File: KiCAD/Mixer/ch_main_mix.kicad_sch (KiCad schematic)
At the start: 1 part, among them U4 NE5532

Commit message: Power Bus, Footprints, Audio Bus
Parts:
- U4: footprint (none) -> Package_SO:SOIC-8_3.9x4.9mm_P1.27mm
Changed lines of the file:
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@@
 			)
 		)
-		(property "Footprint" ""
+		(property "Footprint" "Package_SO:SOIC-8_3.9x4.9mm_P1.27mm"
 			(at 60.96 88.9 0)
 			(hide yes)
@@
 			)
 		)
-		(property "Footprint" ""
+		(property "Footprint" "Package_SO:SOIC-8_3.9x4.9mm_P1.27mm"
 			(at 49.53 49.53 0)
 			(hide yes)
@@
 			)
 		)
-		(property "Footprint" ""
+		(property "Footprint" "Package_SO:SOIC-8_3.9x4.9mm_P1.27mm"
 			(at 60.96 76.2 0)
 			(hide yes)

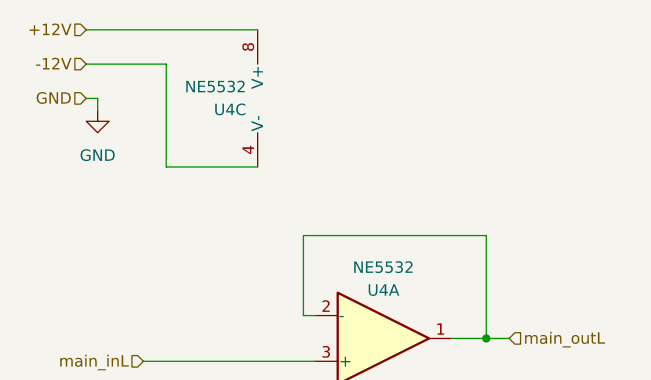
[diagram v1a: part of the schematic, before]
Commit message: added second channel and footprints / created PCB desing...might make PCB bit bigger
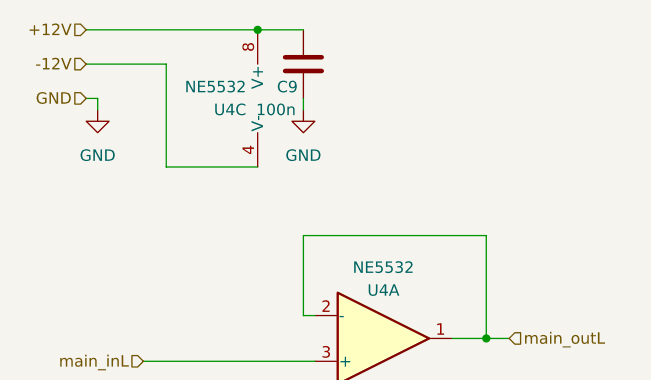
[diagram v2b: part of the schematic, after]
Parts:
- added C9: 100n, Capacitor_SMD:C_0805_2012Metric_Pad1.18x1.45mm_HandSolder, symbol Device:C
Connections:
- net +12V: now also C9.2
- net GND: now also C9.1
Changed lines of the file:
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@@
+	)
+	(junction
+		(at 46.99 41.91)
+		(diameter 0)
+		(color 0 0 0 0)
 	)
 	(junction
@@
 	(wire
 		(pts
+			(xy 46.99 41.91) (xy 52.07 41.91)
+		)
+		(stroke
+			(width 0)
+			(type default)
+		)
+	)
+	(wire
+		(pts
 			(xy 68.58 88.9) (xy 72.39 88.9)
 		)
@@
 		(pts
 			(xy 36.83 57.15) (xy 46.99 57.15)
+		)
+		(stroke
+			(width 0)
+			(type default)
+		)
+	)
+	(wire
+		(pts
+			(xy 52.07 49.53) (xy 52.07 50.8)
 		)
 		(stroke
@@
 		(instances
 			(project "Mixer"
+				(path "/322d427a-6aae-4762-92d6-d97688daf29b/8a2849b7-184d-4014-bb98-da9dec8b5f90/63151d98-ae0a-469c-944a-54e511d723e3"
+					(reference "U6")
+					(unit 2)
+				)
 				(path "/322d427a-6aae-4762-92d6-d97688daf29b/8a2849b7-184d-4014-bb98-da9dec8b5f90/8a6fa50f-425a-481d-926c-437edf9380b2"
 					(reference "U4")
@@
 		(instances
 			(project "Mixer"
+				(path "/322d427a-6aae-4762-92d6-d97688daf29b/8a2849b7-184d-4014-bb98-da9dec8b5f90/63151d98-ae0a-469c-944a-54e511d723e3"
+					(reference "U6")
+					(unit 3)
+				)
 				(path "/322d427a-6aae-4762-92d6-d97688daf29b/8a2849b7-184d-4014-bb98-da9dec8b5f90/8a6fa50f-425a-481d-926c-437edf9380b2"
 					(reference "U4")
 					(unit 3)
+				)
+			)
+		)
+	)
+	(symbol
+		(lib_id "power:GND")
+		(at 52.07 50.8 0)
+		(unit 1)
+		(body_style 1)
+		(exclude_from_sim no)
+		(in_bom yes)
+		(on_board yes)
+		(in_pos_files yes)
+		(dnp no)
+		(fields_autoplaced yes)
+		(property "Reference" "#PWR097"
+			(at 52.07 57.15 0)
+			(hide yes)
+			(show_name no)
+			(do_not_autoplace no)
+			(effects
+				(font
+					(size 1.27 1.27)
+				)
+			)
+		)
+		(property "Value" "GND"
+			(at 52.07 55.88 0)
+			(show_name no)
+			(do_not_autoplace no)
+			(effects
+				(font
+					(size 1.27 1.27)
+				)
+			)
+		)
+		(property "Footprint" ""
+			(at 52.07 50.8 0)
+			(hide yes)
+			(show_name no)
+			(do_not_autoplace no)
+			(effects
+				(font
+					(size 1.27 1.27)
+				)
+			)
+		)
+		(property "Datasheet" ""
+			(at 52.07 50.8 0)
+			(hide yes)
+			(show_name no)
+			(do_not_autoplace no)
+			(effects
+				(font
+					(size 1.27 1.27)
+				)
+			)
+		)
+		(property "Description" "Power symbol creates a global label with name \"GND\" , ground"
+			(at 52.07 50.8 0)
+			(hide yes)
+			(show_name no)
+			(do_not_autoplace no)
+			(effects
+				(font
+					(size 1.27 1.27)
+				)
+			)
+		)
+		(pin "1"
+		)
+		(instances
+			(project "Mixer"
+				(path "/322d427a-6aae-4762-92d6-d97688daf29b/8a2849b7-184d-4014-bb98-da9dec8b5f90/63151d98-ae0a-469c-944a-54e511d723e3"
+					(reference "#PWR098")
+					(unit 1)
+				)
+				(path "/322d427a-6aae-4762-92d6-d97688daf29b/8a2849b7-184d-4014-bb98-da9dec8b5f90/8a6fa50f-425a-481d-926c-437edf9380b2"
+					(reference "#PWR097")
+					(unit 1)
 				)
 			)
@@
 		(instances
 			(project "Mixer"
+				(path "/322d427a-6aae-4762-92d6-d97688daf29b/8a2849b7-184d-4014-bb98-da9dec8b5f90/63151d98-ae0a-469c-944a-54e511d723e3"
+					(reference "U6")
+					(unit 1)
+				)
 				(path "/322d427a-6aae-4762-92d6-d97688daf29b/8a2849b7-184d-4014-bb98-da9dec8b5f90/8a6fa50f-425a-481d-926c-437edf9380b2"
 					(reference "U4")
@@
 		(instances
 			(project "Mixer"
+				(path "/322d427a-6aae-4762-92d6-d97688daf29b/8a2849b7-184d-4014-bb98-da9dec8b5f90/63151d98-ae0a-469c-944a-54e511d723e3"
+					(reference "#PWR094")
+					(unit 1)
+				)
 				(path "/322d427a-6aae-4762-92d6-d97688daf29b/8a2849b7-184d-4014-bb98-da9dec8b5f90/8a6fa50f-425a-481d-926c-437edf9380b2"
 					(reference "#PWR022")
 					(unit 1)
 				)
+			)
+		)
+	)
+	(symbol
+		(lib_id "Device:C")
+		(at 52.07 45.72 180)
+		(unit 1)
+		(body_style 1)
+		(exclude_from_sim no)
+		(in_bom yes)
+		(on_board yes)
+		(in_pos_files yes)
+		(dnp no)
+		(property "Reference" "C9"
+			(at 50.292 48.26 0)
+			(show_name no)
+			(do_not_autoplace no)
+			(effects
+				(font
+					(size 1.27 1.27)
+				)
+			)
+		)
+		(property "Value" "100n"
+			(at 49.022 50.8 0)
+			(show_name no)
+			(do_not_autoplace no)
+			(effects
+				(font
+					(size 1.27 1.27)
+				)
+			)
+		)
+		(property "Footprint" "Capacitor_SMD:C_0805_2012Metric_Pad1.18x1.45mm_HandSolder"
+			(at 51.1048 41.91 0)
+			(hide yes)
+			(show_name no)
+			(do_not_autoplace no)
+			(effects
+				(font
+					(size 1.27 1.27)
+				)
+			)
+		)
+		(property "Datasheet" ""
+			(at 52.07 45.72 0)
+			(hide yes)
+			(show_name no)
+			(do_not_autoplace no)
+			(effects
+				(font
+					(size 1.27 1.27)
+				)
+			)
+		)
+		(property "Description" "Unpolarized capacitor"
+			(at 52.07 45.72 0)
+			(hide yes)
+			(show_name no)
+			(do_not_autoplace no)
+			(effects
+				(font
+					(size 1.27 1.27)
+				)
+			)
+		)
+		(pin "1"
+		)
+		(pin "2"
+		)
+		(instances
+			(project "Mixer"
+				(path "/322d427a-6aae-4762-92d6-d97688daf29b/8a2849b7-184d-4014-bb98-da9dec8b5f90/63151d98-ae0a-469c-944a-54e511d723e3"
+					(reference "C10")
+					(unit 1)
+				)
+				(path "/322d427a-6aae-4762-92d6-d97688daf29b/8a2849b7-184d-4014-bb98-da9dec8b5f90/8a6fa50f-425a-481d-926c-437edf9380b2"
+					(reference "C9")
+					(unit 1)
+				)

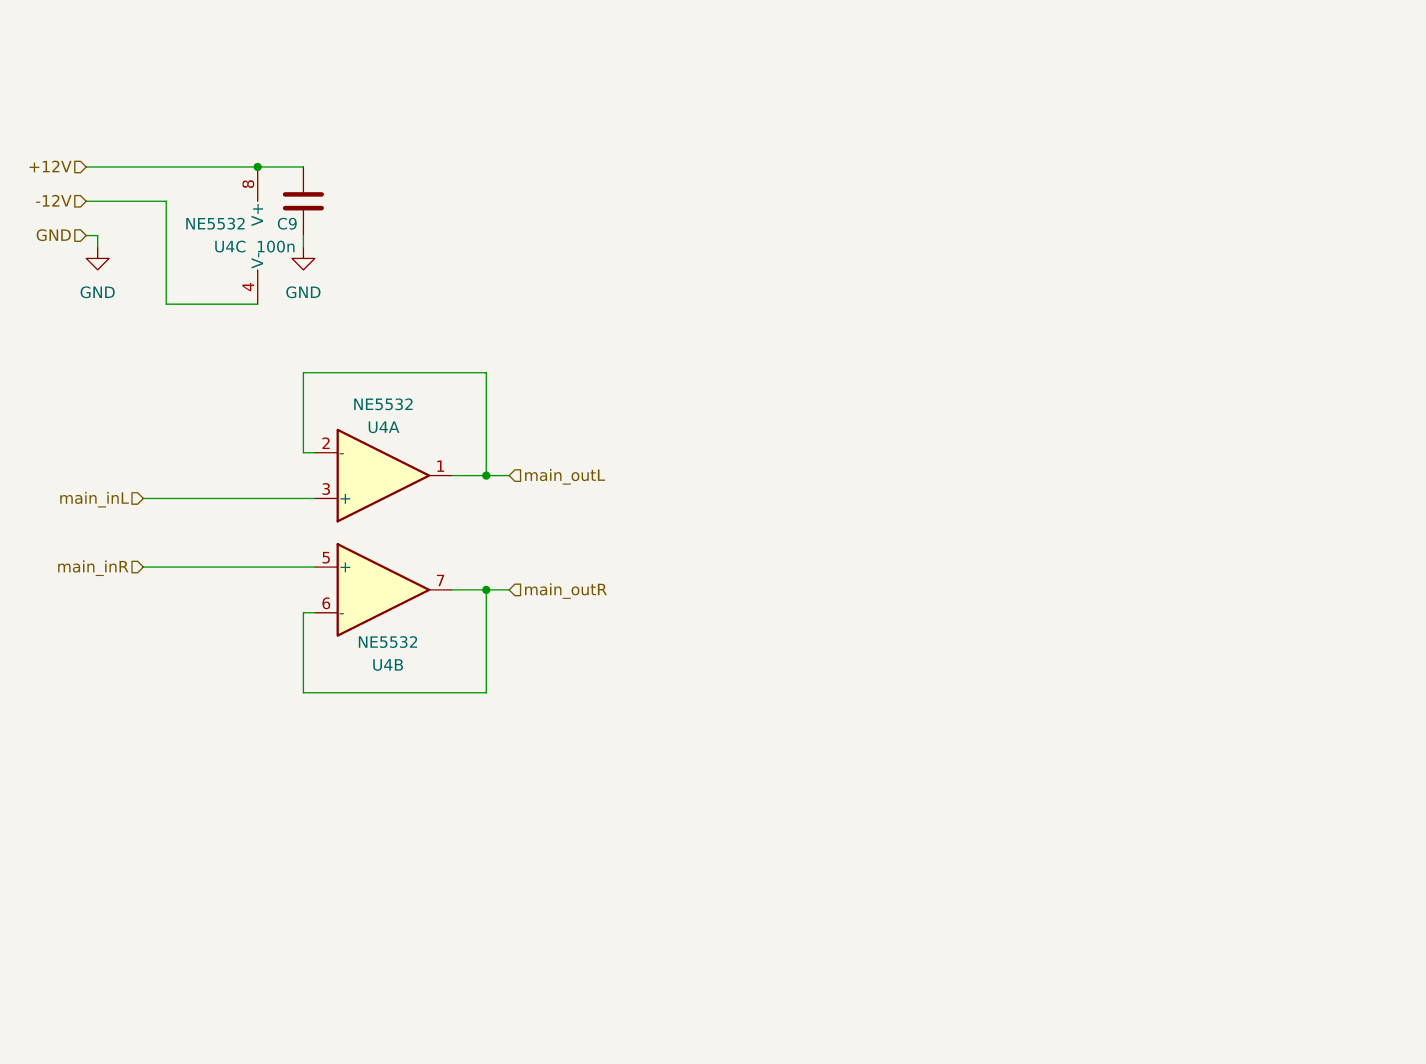
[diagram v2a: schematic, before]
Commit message: Cs an OPV-Strom, Anpassung clicklessmute,...
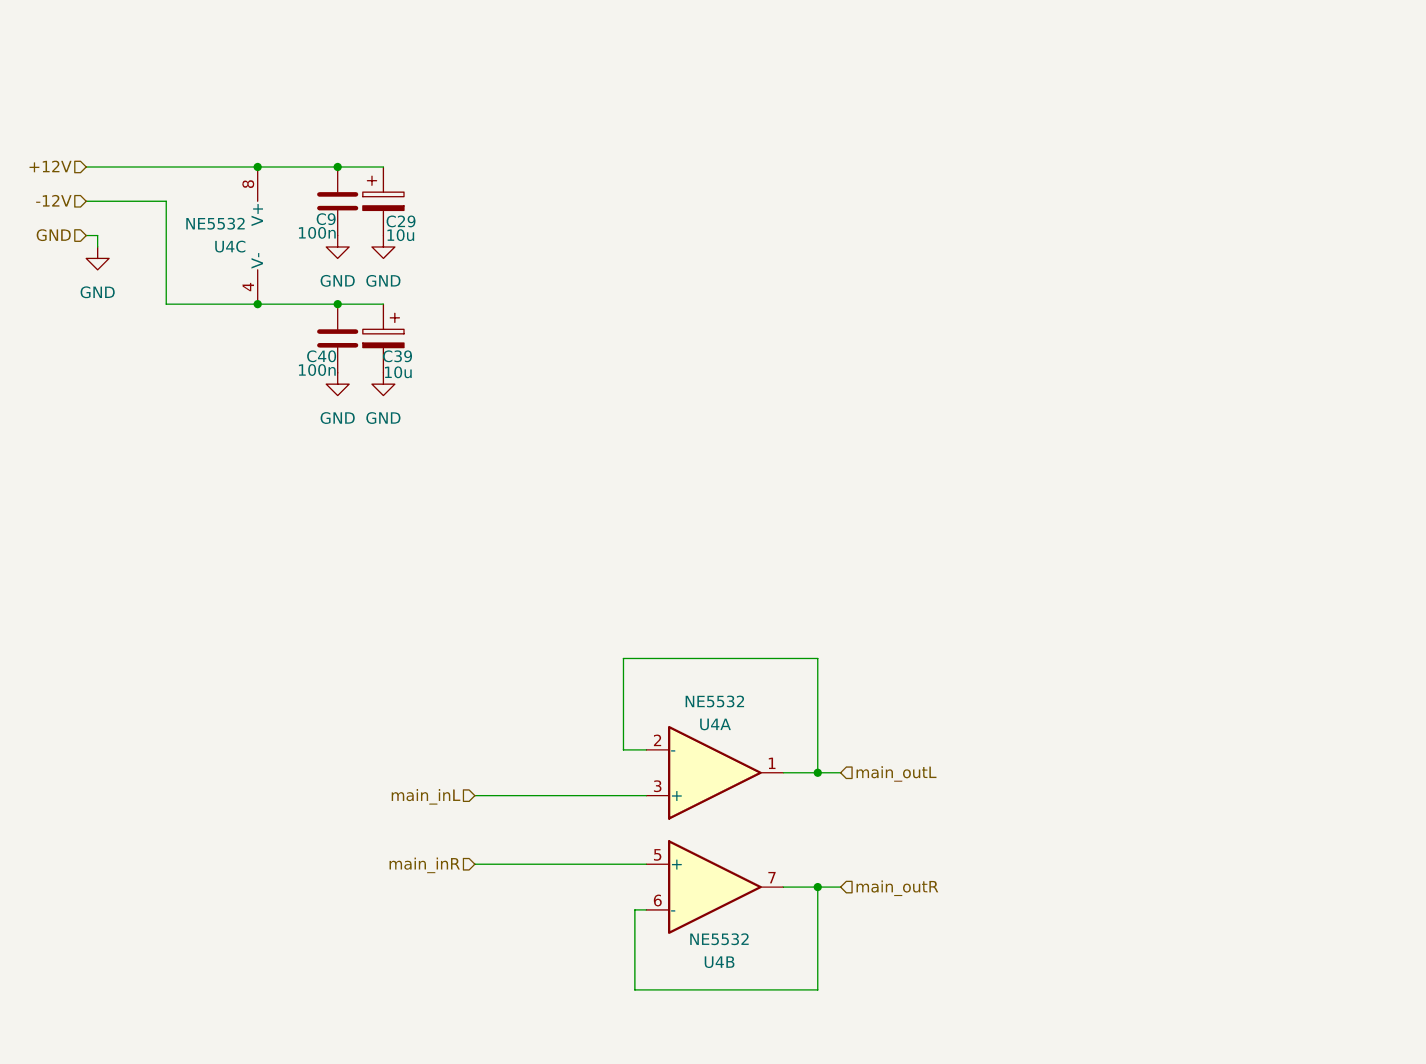
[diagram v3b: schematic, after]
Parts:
- added C29, C39: 10u, Capacitor_SMD:CP_Elec_10x10, symbol Device:C_Polarized
- added C40: 100n, Capacitor_SMD:C_0805_2012Metric_Pad1.18x1.45mm_HandSolder, symbol Device:C
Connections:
- net +12V: now also C29.1
- net -12V: now also C39.1, C40.2
- net GND: now also C29.2, C39.2, C40.1
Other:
- moved on the sheet: C9, U4A, U4B

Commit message: überarbeitete Schaltung und PCB Desing...v1.0 FERTIG
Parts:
- removed C29, C39: 10u, Capacitor_SMD:CP_Elec_10x10, symbol Device:C_Polarized
- added C10, C41: 100n, Capacitor_SMD:C_0805_2012Metric_Pad1.18x1.45mm_HandSolder, symbol Device:C
- added R29, R30, R31, R32, R33, R34, R35, R36, R37, R38, R41, R42: 1k, Resistor_SMD:R_0805_2012Metric_Pad1.20x1.40mm_HandSolder, symbol Device:R
- added U5: NE5532, Package_SO:SOIC-8_3.9x4.9mm_P1.27mm, symbol Amplifier_Operational:NE5532
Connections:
- net main_inL is gone; now on net GND: U4.3 (+)
- net main_inR is gone; now on net GND: U4.5 (+)
- net +12V: now also C10.2, U5.8 (V+)
- net -12V: now also C41.2, U5.4 (V-)
- net GND: now also C10.1, C41.1, U5.3 (+), U5.5 (+)
- net main_outL: now also R37.2, U5.1; no longer U4.1, U4.2 (-)
- net main_outR: now also R38.2, U5.7; no longer U4.6 (-), U4.7
- new net: R38.1, R41.2, U5.6 (-)
- new net: R29.2, R42.1, U4.1
- new net: R37.1, R42.2, U5.2 (-)
- new net: R29.1, R33.2, R34.2, R35.2, U4.2 (-)
- new net: R30.1, R31.2, R32.2, R36.2, U4.6 (-)
- new net: R30.2, R41.1, U4.7
- new net main_inL1: R34.1
- new net main_inL2: R33.1
- new net main_inR1: R31.1
- new net main_inR2: R32.1
- new net pre_mixL: R35.1
- new net pre_mixR: R36.1

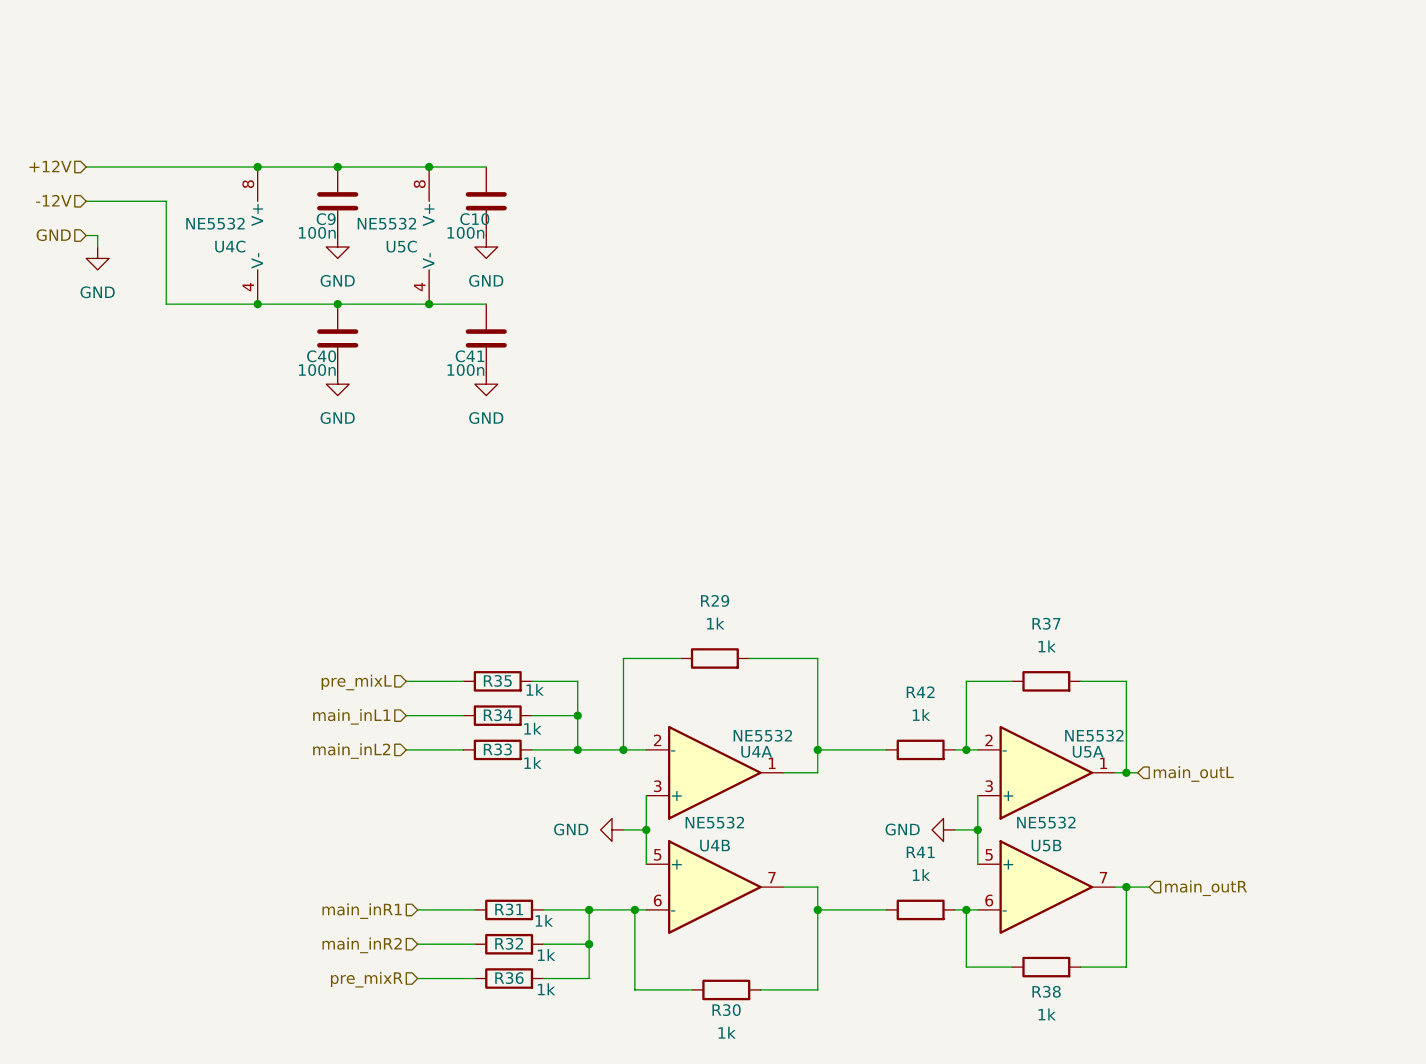
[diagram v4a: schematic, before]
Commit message: Rework of schematic, with error fixes and reworked pcb
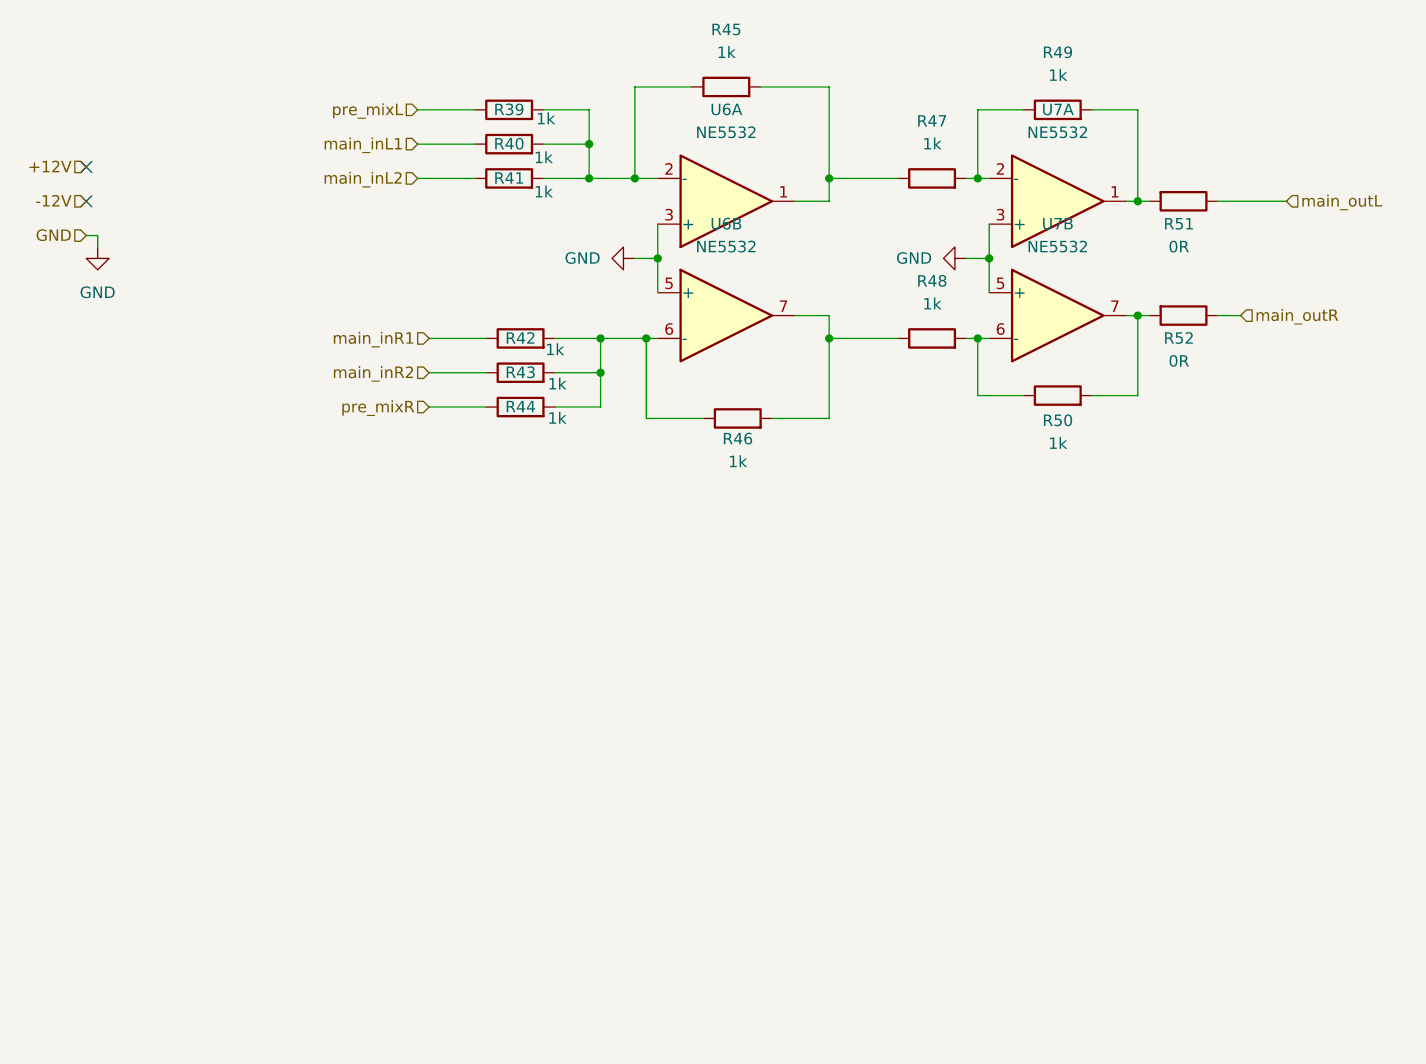
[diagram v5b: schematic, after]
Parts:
- removed C10, C40, C41, C9: 100n, Capacitor_SMD:C_0805_2012Metric_Pad1.18x1.45mm_HandSolder, symbol Device:C
- removed U4, U5: NE5532, Package_SO:SOIC-8_3.9x4.9mm_P1.27mm, symbol Amplifier_Operational:NE5532
- added R51, R52: 0R, Resistor_SMD:R_0805_2012Metric_Pad1.20x1.40mm_HandSolder, symbol Device:R
- added U6, U7: NE5532, Package_SO:SOIC-8_3.9x4.9mm_P1.27mm, symbol Amplifier_Operational:NE5532
- renumbered R35 to R39, R34 to R40, R33 to R41, R31 to R42, R32 to R43, R36 to R44, R29 to R45, R30 to R46, R42 to R47, R41 to R48, R37 to R49, R38 to R50
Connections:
- net GND: now also U6.3 (+), U6.5 (+), U7.3 (+), U7.5 (+)
- net main_outL: now also R51.1; no longer R49.2
- net main_outR: now also R52.1; no longer R50.2
- net at R48.2, R50.1: now also U7.6 (-)
- net at R45.2, R47.1: now also U6.1
- net at R47.2, R49.1: now also U7.2 (-)
- net at R39.2, R40.2, R41.2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: now also U6.2 (-)
- net at R42.2, R43.2, R44.2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: now also U6.6 (-)
- net at R46.2, R48.1: now also U6.7
- new net: R49.2, R51.2, U7.1
- new net: R50.2, R52.2, U7.7
- no-connect marks 0 -> 2
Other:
- moved on the sheet: R39, R40, R41, R42, R43, R44, R45, R46, R47, R48, R49, R50
